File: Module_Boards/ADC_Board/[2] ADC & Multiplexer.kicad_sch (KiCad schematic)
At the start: 11 parts, among them J1 212134-0003, J2 212134-0003, J3 212134-0003, J4 212134-0003, U1 LTC1864LIMS8#PBF, U5 TMUX1104DQAR

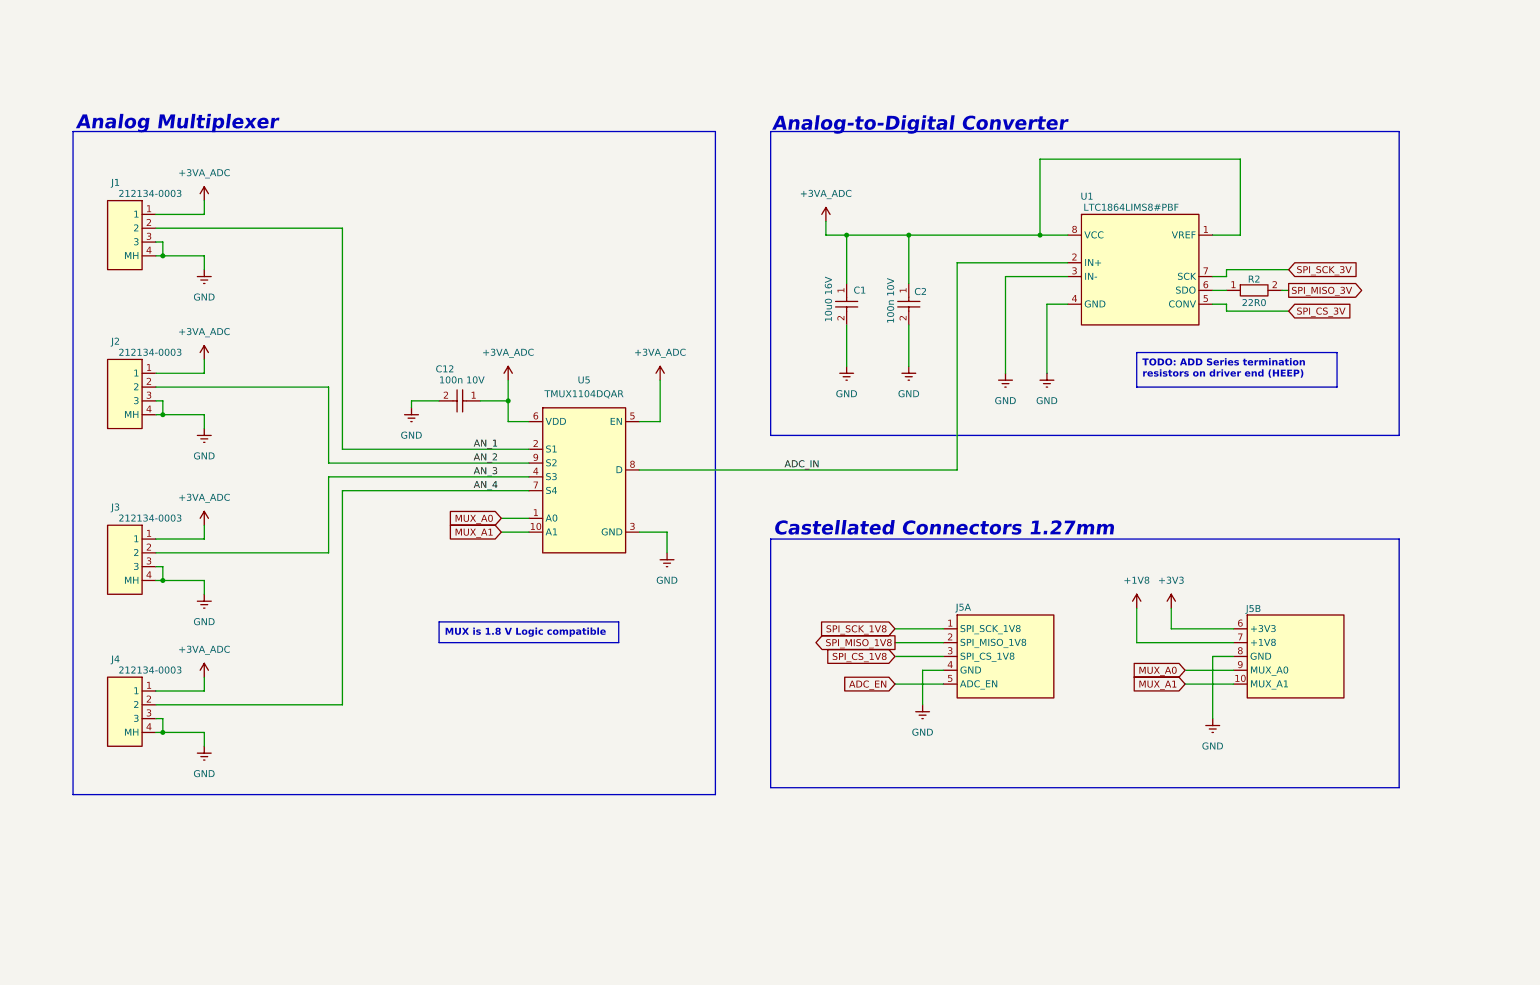
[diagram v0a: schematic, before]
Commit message: Fixed bugs. Added comments. Push before changing the ADC
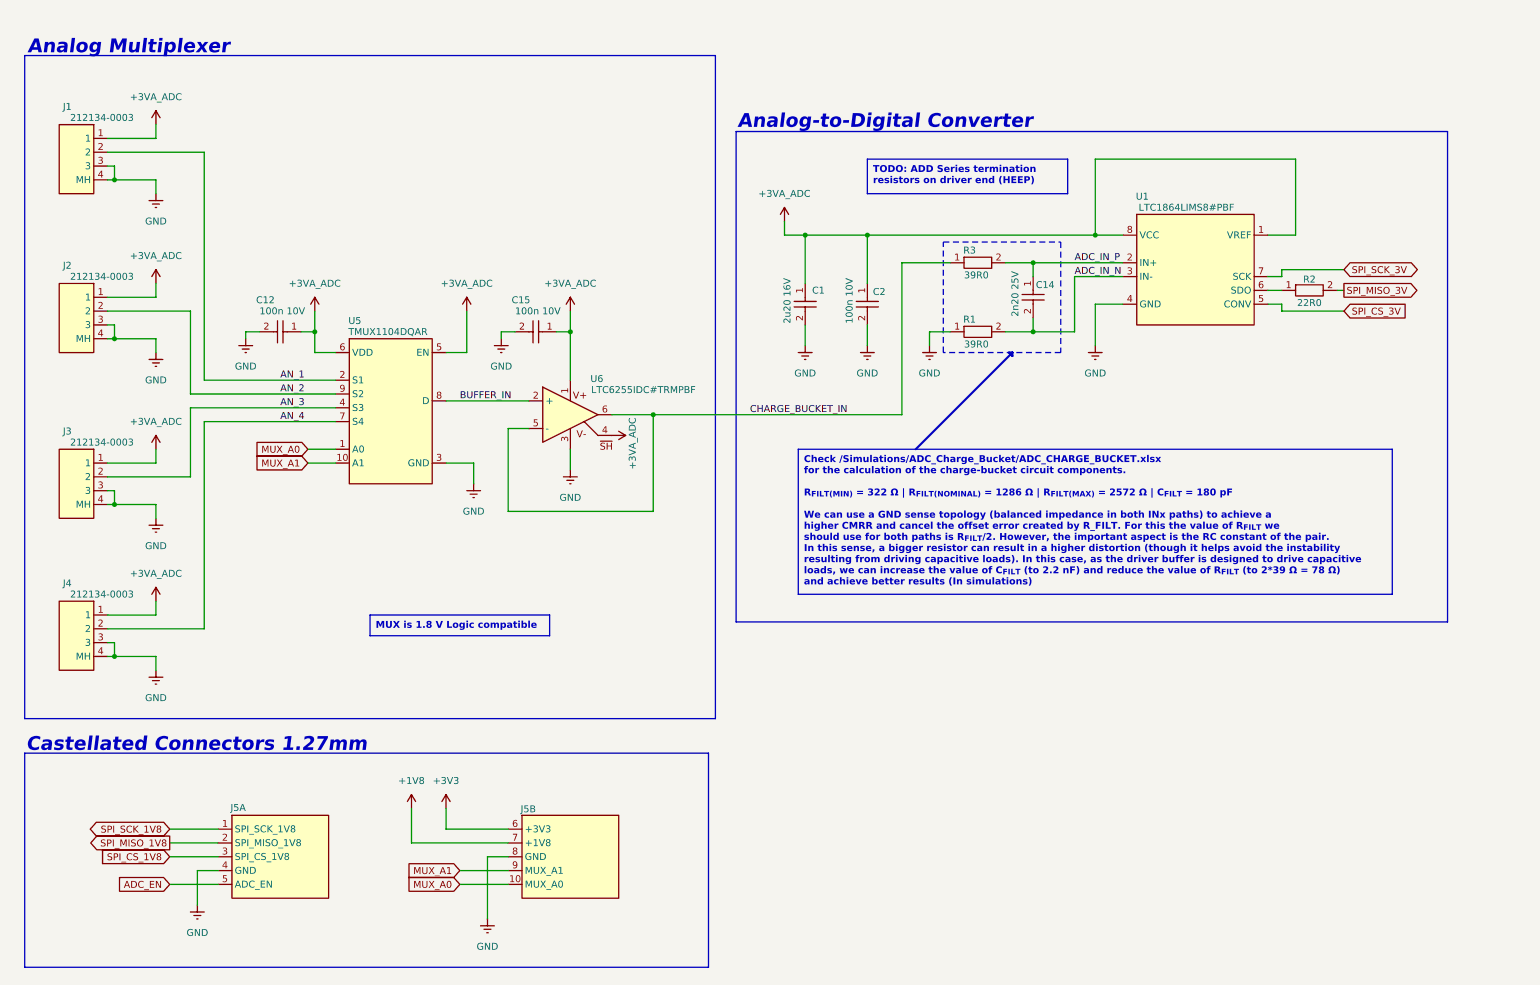
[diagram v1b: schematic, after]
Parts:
- added C14: 2n20 25V, X-MODs_PcbLib:C0402, symbol X-MODs_SchLib:C0402C222F3GACTU
- added C15: 100n 10V, X-MODs_PcbLib:C0402, symbol X-MODs_SchLib:GRM155R71A104JA01D
- added R1, R3: 39R0, X-MODs_PcbLib:R0402, symbol X-MODs_SchLib:RT0402BRD0739RL
- added U6: LTC6255IDC#TRMPBF, X-MODs_PcbLib:DFN-6, symbol X-MODs_SchLib:LTC6255IDC#TRMPBF
- C1: value 10u0 16V -> 2u20 16V; symbol X-MODs_SchLib:GRM155R60G106ME01D -> X-MODs_SchLib:GRM155R61C225KE44D; MPN GRM155R60G106ME01D -> GRM155R61C225KE44D
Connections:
- net +3VA_ADC: now also C15.1, U6.1 (V+), U6.4 (~{SH})
- net GND: now also C15.2, R1.1, U6.3 (V-); no longer U1.3 (IN-)
- net MUX_A0: now also J5.10 (MUX_A0); no longer J5.9 (MUX_A0)
- net MUX_A1: now also J5.9 (MUX_A1); no longer J5.10 (MUX_A1)
- net ADC_IN renamed ADC_IN_P
- net ADC_IN_P: now also C14.1, R3.2; no longer U5.8 (D)
- new net ADC_IN_N: C14.2, R1.2, U1.3 (IN-)
- new net BUFFER_IN: U5.8 (D), U6.2 (+)
- new net CHARGE_BUCKET_IN: R3.1, U6.5 (-), U6.6 (VOUT)
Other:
- company: (none) -> Embedded Systems Laboratory - EPFL
- title: (none) -> [2] ADC & Multiplexer
- moved on the sheet: C1, C12, C2, J1, J2, J3, J4, J5A, J5B, R2, U1, U5

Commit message: Added new version of the ADC Board. Better ADC, precision reference. Similar power consumption
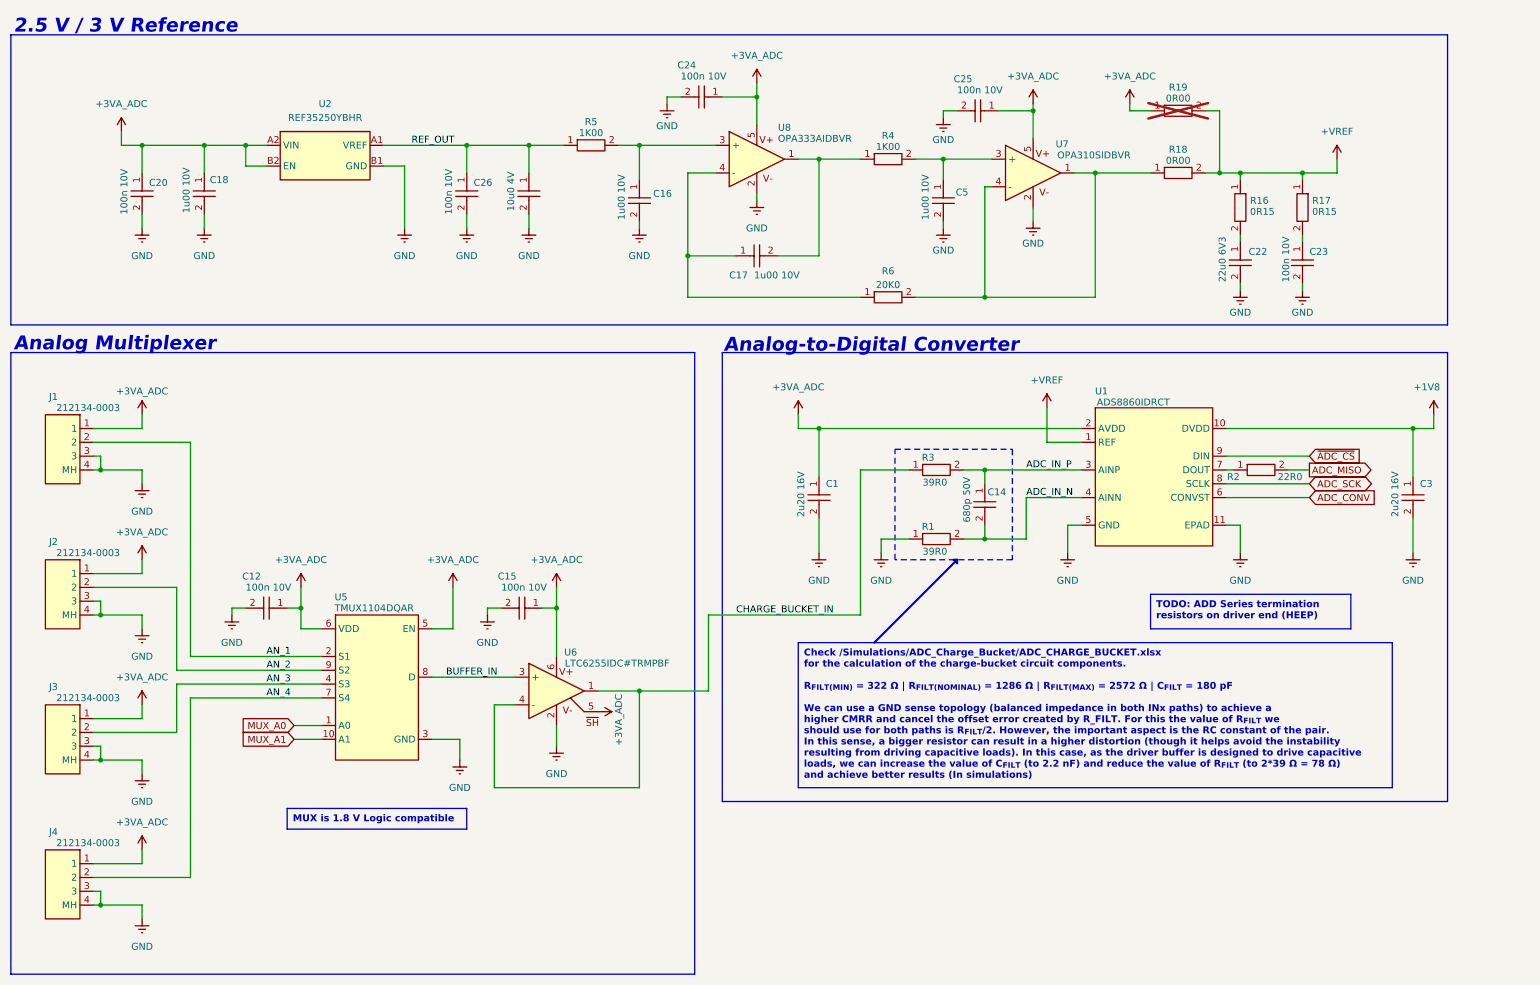
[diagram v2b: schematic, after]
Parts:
- removed C2: 100n 10V, X-MODs_PcbLib:C0402, symbol X-MODs_SchLib:GRM155R71A104JA01D
- removed J5: ~, X-MODs_PcbLib:ADC_Board_Castellated_Conn_1.27mm, symbol X-MODs_SchLib:ADC_Board_Castellated_Conn_1.27mm
- removed U1: LTC1864LIMS8#PBF, X-MODs_PcbLib:MSOP-8, symbol X-MODs_SchLib:LTC1864LIMS8#PBF
- added C16, C17, C18, C5: 1u00 10V, X-MODs_PcbLib:C0402, symbol X-MODs_SchLib:C0402C105K8PACTU
- added C20, C23, C24, C25, C26: 100n 10V, X-MODs_PcbLib:C0402, symbol X-MODs_SchLib:GRM155R71A104JA01D
- added C21: 10u0 4V, X-MODs_PcbLib:C0402, symbol X-MODs_SchLib:GRM155R60G106ME01D
- added C22: 22u0 6V3, X-MODs_PcbLib:C0402, symbol X-MODs_SchLib:CL05A226MQ5CUN
- added C3: 2u20 16V, X-MODs_PcbLib:C0402, symbol X-MODs_SchLib:GRM155R61C225KE44D
- added R16, R17: 0R15, X-MODs_PcbLib:R0402, symbol X-MODs_SchLib:KDV04FR150ET
- added R18, R19: 0R00, X-MODs_PcbLib:R0402, symbol X-MODs_SchLib:RK73Z1ETTP
- added R4, R5: 1K00, X-MODs_PcbLib:R0402, symbol X-MODs_SchLib:ERA-2ARC102X
- added R6: 20K0, X-MODs_PcbLib:R0402, symbol X-MODs_SchLib:ERA-2ARC203X
- added U1: ADS8860IDRCT, X-MODs_PcbLib:VSON-10_3x3mm_P0.5, symbol X-MODs_SchLib:ADS8860IDRCT
- added U2: REF35250YBHR, X-MODs_PcbLib:DSBGA-4_1.085x0.870mm, symbol X-MODs_SchLib:REF35250YBHR
- added U7: OPA310SIDBVR, X-MODs_PcbLib:SOT_23_5_SHDN, symbol X-MODs_SchLib:OPA310SIDBVR
- added U8: OPA333AIDBVR, X-MODs_PcbLib:SOT_23_5_SHDN, symbol X-MODs_SchLib:OPA333AIDBVR
- C14: value 2n20 25V -> 680p 50V; symbol X-MODs_SchLib:C0402C222F3GACTU -> X-MODs_SchLib:GCM1555C1H681FA16J; MPN C0402C222F3GACTU -> GCM1555C1H681FA16J
- U6: footprint X-MODs_PcbLib:DFN-6 -> X-MODs_PcbLib:SOT_23_6; symbol X-MODs_SchLib:LTC6255IDC#TRMPBF -> X-MODs_SchLib:LTC6255CS6#TRMPBF; MPN LTC6255IDC#TRMPBF -> LTC6255CS6#TRMPBF
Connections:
- net +1V8: now also C3.1, U1.10 (DVDD)
- net +3VA_ADC: now also U6.5 (~{SH}), U6.6 (V+), C18.1, C20.1, C24.1, C25.1, R19.1, U1.2 (AVDD), U2.A2 (VIN), U2.B2 (EN), U7.5 (V+), U8.5 (V+); no longer U6.1 (V+), U6.4 (~{SH})
- net ADC_IN_N: now also U1.4 (AINN)
- net ADC_IN_P: now also U1.3 (AINP)
- net BUFFER_IN: now also U6.3 (+); no longer U6.2 (+)
- net CHARGE_BUCKET_IN: now also U6.1 (VOUT), U6.4 (-); no longer U6.5 (-), U6.6 (VOUT)
- net GND: now also U6.2 (V-), C16.2, C18.2, C20.2, C21.2, C22.2, C23.2, C24.2, C25.2, C26.2, C3.2, C5.2, U1.11 (EPAD), U1.5 (GND), U2.B1 (GND), U7.2 (V-), U8.2 (V-); no longer U6.3 (V-)
- net at R2.1: now also U1.7 (DOUT)
- net SPI_MISO_3V renamed ADC_MISO
- new net: C5.1, R4.2, U7.3 (+)
- new net: C16.1, R5.2, U8.3 (+)
- new net: C17.1, R6.1, U8.4 (-)
- new net: C17.2, R4.1, U8.1 (VOUT)
- new net: R18.1, R6.2, U7.1 (VOUT), U7.4 (-)
- new net: C22.1, R16.2
- new net: C23.1, R17.2
- new net +VREF: R16.1, R17.1, R18.2, R19.2, U1.1 (REF)
- new net ADC_CONV: U1.6 (CONVST)
- new net ADC_SCK: U1.8 (SCLK)
- new net REF_OUT: C21.1, C26.1, R5.1, U2.A1 (VREF)
- new net ~{ADC_CS}: U1.9 (DIN)
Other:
- note added: "2.5 V / 3 V Reference"
- note removed: "Castellated Connectors 1.27mm"
- moved on the sheet: C1, C12, C14, C15, J1, J2, J3, J4, R1, R3, U5, U6
